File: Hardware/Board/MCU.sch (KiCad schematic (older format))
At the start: 41 parts, among them J3 USB_B_Micro, J5 Conn_ARM_JTAG_SWD_20, SW1 SW_Push, U2 AT25SF081-XMHD-X, Y1 16MHz, Y2 32.768

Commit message: Port Bezeichnungen am Prozessor korrigiert, Schnittstellen angepasst.
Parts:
- removed U2: AT25SF081-XMHD-X, Package_SO:TSSOP-8_4.4x3mm_P0.65mm, symbol Memory_Flash:AT25SF081-XMHD-X
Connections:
- net labels added: CAN1_RX, CAN1_TX, ESP_Boot, ESP_Enable, ESP_Reset, ESP_RxD, ESP_TxD, I2C2_SCL, I2C2_SDA, I2C3_SCL, I2C3_SDA, I2C4_SCL, I2C4_SDA, LPUART_RTS_DE_RS485, LPUART_RX_RX485, LPUART_TX_RS485, OctoSPI_P1_CLK, OctoSPI_P1_DQS, OctoSPI_P1_IO0, OctoSPI_P1_IO1, OctoSPI_P1_IO2, OctoSPI_P1_IO3, OctoSPI_P1_IO4, OctoSPI_P1_IO5, OctoSPI_P1_IO6, OctoSPI_P1_IO7, OctoSPI_P1_NCS, OctoSPI_P2_CLK, OctoSPI_P2_DQS, OctoSPI_P2_IO0, OctoSPI_P2_IO1, OctoSPI_P2_IO2, OctoSPI_P2_IO3, OctoSPI_P2_IO4, OctoSPI_P2_IO5, OctoSPI_P2_IO6, OctoSPI_P2_IO7, OctoSPI_P2_NCS, SLP-LIN1, SLP-LIN2, SLP-LIN3, SPI1_MISO, SPI1_MOSI, SPI1_NSS, SPI1_SCK, STB-CAN, UART4_RX, UART4_TX, UART5_RX, UART5_TX, USART1_RX_LIN1, USART1_TX_LIN1, USART2_RX_LIN2, USART2_TX_LIN2, USART3_RX_LIN3, USART3_TX_LIN3
- net labels removed: Disp_Audio_L, Disp_MOSI, Disp_SCK, OctoSPI_CLK, OctoSPI_DQS, OctoSPI_IO0, OctoSPI_IO1, OctoSPI_IO2, OctoSPI_IO3, OctoSPI_IO4, OctoSPI_IO5, OctoSPI_IO6, OctoSPI_IO7, OctoSPI_NCS, QuadSPI_CLK, QuadSPI_IO0, QuadSPI_IO1, QuadSPI_IO2, QuadSPI_IO3, QuadSPI_NCS, RxD-CAN, RxD-LIN1, RxD-LIN2, RxD-LIN3, RxD-RS485, SCL-1WIRE, SDA-1WIRE, TOUCH_SCL, TOUCH_SDA, TxD-CAN, TxD-LIN1, TxD-LIN2, TxD-LIN3, TxD-RS485
- wire segments 253 -> 291
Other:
- moved on the sheet: D3, J3, U?

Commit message: Octo SPI Flash und RAM zugefügt, weitere Bezeichnungen auf Stand gebracht
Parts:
- removed C14: 100nF, Capacitor_SMD:C_0603_1608Metric, symbol Device:C
- added C? (x6): 100nF, Capacitor_SMD:C_0603_1608Metric, symbol Device:C
- added IC?: IS66WVH8M8BLL-100B1LI_0, BGA24C100P5X5_600X800X120, symbol SamacSys_Parts:IS66WVH8M8BLL-100B1LI_0
- added IC?: MX25LM51245GXDI00, BGA24C100P5X5_600X800X35, symbol SamacSys_Parts:MX25LM51245GXDI00
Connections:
- net labels added: +VSW, LCD_BL_CTRL, LCD_INT, RESET
- net labels removed: Disp_CS, Disp_INT, Disp_MISO
- wire segments 291 -> 334
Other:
- moved on the sheet: D2, D3, J3, J5, U?

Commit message: Eine Menge Arbeit auf der GPN, fast fertig im Schaltplan.
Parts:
- removed D1, D2, D3: SP0504BAJT, Package_TO_SOT_SMD:SOT-353_SC-70-5, symbol Power_Protection:SP0504BAJT
- IC?: symbol SamacSys_Parts:IS66WVH8M8BLL-100B1LI_0 -> Womo-rescue:IS66WVH8M8BLL-100B1LI_0-SamacSys_Parts
- IC?: symbol SamacSys_Parts:MX25LM51245GXDI00 -> Womo-rescue:MX25LM51245GXDI00-SamacSys_Parts
- J?: symbol SamacSys_Parts:54104-4031 -> Womo-rescue:54104-4031-SamacSys_Parts
- J?: symbol SamacSys_Parts:52271-0679 -> Womo-rescue:52271-0679-SamacSys_Parts
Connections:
- net labels added: BLE_INT, Rasp_Shutdown, Rasp_down
- net labels removed: +5VL, BLE_MISO, BLE_MOSI, BLE_RDNY, BLE_REQN, BLE_SCK, Disp_PD, ESP_RxD, ESP_TxD, SLP-LIN1, SLP-LIN2, SLP-LIN3, STB-CAN
- wire segments 334 -> 347
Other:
- moved on the sheet: J3, U?

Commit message: Board to Board Verbindung eingefügt
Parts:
- added C?: 10u, Capacitor_SMD:C_1210_3225Metric, symbol Device:C
- added J?: Conn_02x25_Odd_Even, Connector_PinHeader_2.54mm:PinHeader_2x25_P2.54mm_Vertical, symbol Connector_Generic:Conn_02x25_Odd_Even
- added U?: MOD-nRF8001, RF_Module:MOD-nRF8001, symbol RF_Bluetooth:MOD-nRF8001
- IC1: renamed from IC?; footprint BGA24C100P5X5_600X800X35 -> (none)
- IC2: renamed from IC?; footprint BGA24C100P5X5_600X800X120 -> (none)
- J14: renamed from J?; footprint 52271-0679 -> (none)
- J4: renamed from J?; footprint 54104-4031 -> (none)
- gave numbers to parts that had none: 21
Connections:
- net BLE_Active: now also U?.11 (ACTIVE)
- net BLE_INT: now also U?.10 (RDYN)
- net GND: now also C?.2, J?.43 (Pin_43), J?.44 (Pin_44), J?.49 (Pin_49), J?.50 (Pin_50), U?.2 (GND)
- net LCD_LED-A: now also J?.46 (Pin_46), J?.48 (Pin_48)
- net LCD_LED-K: now also J?.45 (Pin_45), J?.47 (Pin_47)
- net SPI1_MISO: now also U?.9 (MISO)
- net SPI1_MOSI: now also U?.8 (MOSI)
- net SPI1_NSS: now also U?.7 (REQN)
- net SPI1_SCK: now also U?.6 (SCK)
- net PA9: now reaches U17.103 (PA9)
- net PB2: now reaches U17.44 (PB2)
- net PF11: now reaches U17.45 (PF11)
- new net +3.3VA: C?.1, U?.1 (3V3)
- new net BLE_RST: U?.3 (RST)
- no-connect marks 0 -> 2
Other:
- note added: "Connection to Mainboard"
- moved on the sheet: BT1, C1, C10, C11, C12, C13, C15, C2, C3, C4, C5, C6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

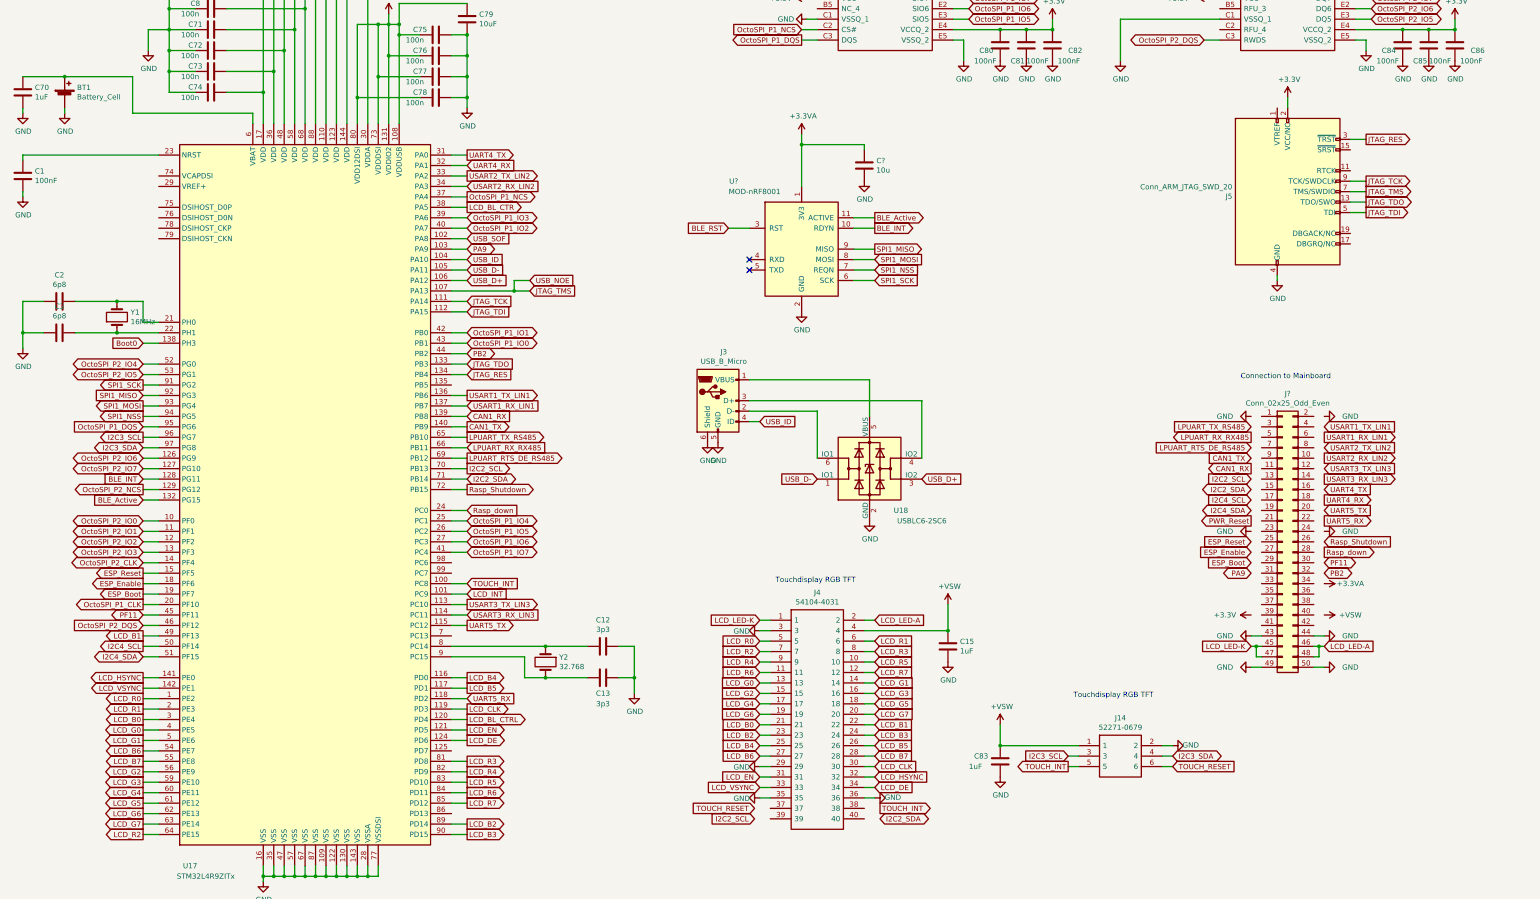
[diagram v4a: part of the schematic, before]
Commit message: Resitiven Touch Controller eingefügt, diverse I2C Parts hinzu gefügt, Netze umgenannt
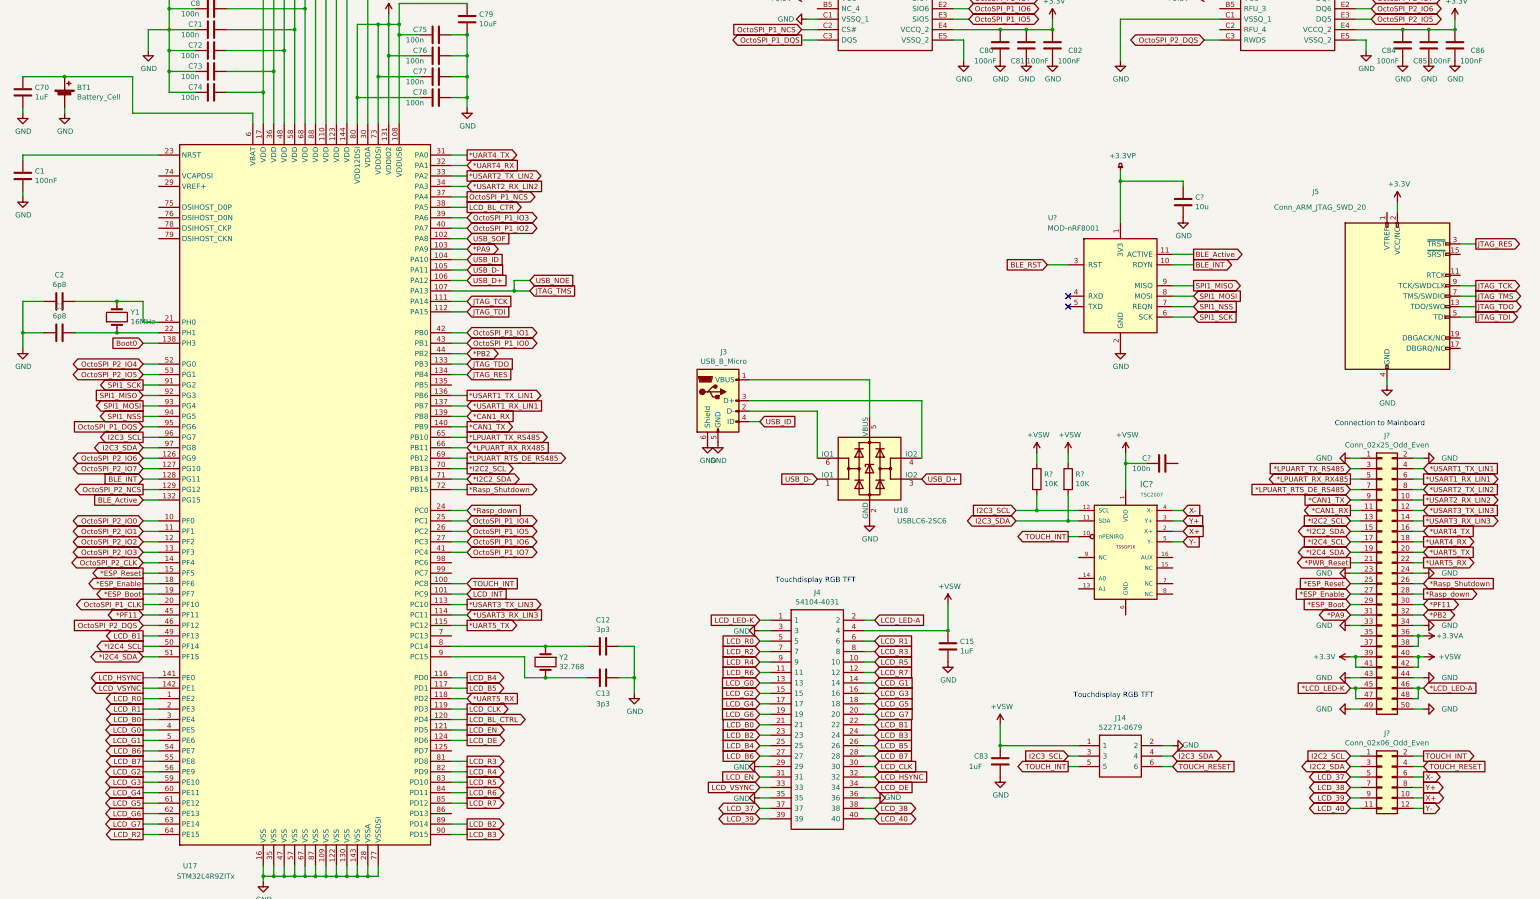
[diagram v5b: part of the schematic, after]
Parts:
- added C?: 100n, Capacitor_SMD:C_0603_1608Metric, symbol Device:C
- added IC?: TSC2007, symbol opendous:TSC2007
- added J?: Conn_02x06_Odd_Even, symbol Connector_Generic:Conn_02x06_Odd_Even
- added R? (x2): 10K, Resistor_SMD:R_0603_1608Metric, symbol Device:R
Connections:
- net CAN1_RX is gone; now on net *CAN1_RX: U17.139 (PB8)
- net CAN1_TX is gone; now on net *CAN1_TX: U17.140 (PB9)
- net ESP_Boot is gone; now on net *ESP_Boot: U17.19 (PF7)
- net ESP_Enable is gone; now on net *ESP_Enable: U17.18 (PF6)
- net ESP_Reset is gone; now on net *ESP_Reset: U17.15 (PF5)
- net I2C4_SCL is gone; now on net *I2C4_SCL: U17.50 (PF14)
- net I2C4_SDA is gone; now on net *I2C4_SDA: U17.51 (PF15)
- net LPUART_RTS_DE_RS485 is gone; now on net *LPUART_RTS_DE_RS485: U17.69 (PB12)
- net LPUART_RX_RX485 is gone; now on net *LPUART_RX_RX485: U17.66 (PB11)
- net LPUART_TX_RS485 is gone; now on net *LPUART_TX_RS485: U17.65 (PB10)
- net PA9 is gone; now on net *PA9: U17.103 (PA9)
- net PB2 is gone; now on net *PB2: U17.44 (PB2)
- net PF11 is gone; now on net *PF11: U17.45 (PF11)
- net Rasp_Shutdown is gone; now on net *Rasp_Shutdown: U17.72 (PB15)
- net Rasp_down is gone; now on net *Rasp_down: U17.24 (PC0)
- net UART4_RX is gone; now on net *UART4_RX: U17.32 (PA1)
- net UART4_TX is gone; now on net *UART4_TX: U17.31 (PA0)
- net UART5_RX is gone; now on net *UART5_RX: U17.118 (PD2)
- net UART5_TX is gone; now on net *UART5_TX: U17.115 (PC12)
- net USART1_RX_LIN1 is gone; now on net *USART1_RX_LIN1: U17.137 (PB7)
- net USART1_TX_LIN1 is gone; now on net *USART1_TX_LIN1: U17.136 (PB6)
- net USART2_RX_LIN2 is gone; now on net *USART2_RX_LIN2: U17.34 (PA3)
- net USART2_TX_LIN2 is gone; now on net *USART2_TX_LIN2: U17.33 (PA2)
- net USART3_RX_LIN3 is gone; now on net *USART3_RX_LIN3: U17.114 (PC11)
- net USART3_TX_LIN3 is gone; now on net *USART3_TX_LIN3: U17.113 (PC10)
- net +3.3VA: now also J?.36 (Pin_36), J?.38 (Pin_38); no longer C?.1, U?.1 (3V3)
- net +3V3: now also J?.39 (Pin_39), J?.41 (Pin_41)
- net +VSW: now also J?.40 (Pin_40), J?.42 (Pin_42), C?.2, IC?.1 (VDD), R?.1, R?.1
- net GND: now also J?.1 (Pin_1), J?.2 (Pin_2), J?.23 (Pin_23), J?.24 (Pin_24), J?.33 (Pin_33), J?.34 (Pin_34)
- net I2C2_SCL: now also J?.1 (Pin_1); no longer U17.70 (PB13)
- net I2C2_SDA: now also J?.3 (Pin_3); no longer U17.71 (PB14)
- net I2C3_SCL: now also IC?.12 (SCL), R?.2
- net I2C3_SDA: now also IC?.11 (SDA), R?.2
- net LCD_LED-A: no longer J?.46 (Pin_46), J?.48 (Pin_48)
- net LCD_LED-K: no longer J?.45 (Pin_45), J?.47 (Pin_47)
- net TOUCH_INT: now also IC?.10 (nPENIRQ), J?.2 (Pin_2)
- net TOUCH_RESET: now also J?.4 (Pin_4)
- net LCD_37: now reaches J4.37
- net LCD_37: now also J?.5 (Pin_5)
- net LCD_38: now reaches J4.38
- net LCD_38: now also J?.7 (Pin_7)
- net LCD_39: now reaches J4.39
- net LCD_39: now also J?.9 (Pin_9)
- net LCD_40: now reaches J4.40
- net LCD_40: now also J?.11 (Pin_11)
- net *USART2_RX_LIN2: now reaches J?.10 (Pin_10)
- net *CAN1_RX: now reaches J?.11 (Pin_11)
- net *USART3_TX_LIN3: now reaches J?.12 (Pin_12)
- net *I2C2_SCL: now reaches J?.13 (Pin_13)
- net *I2C2_SCL: now also U17.70 (PB13)
- net *USART3_RX_LIN3: now reaches J?.14 (Pin_14)
- net *I2C2_SDA: now reaches J?.15 (Pin_15)
- net *I2C2_SDA: now also U17.71 (PB14)
- net *UART4_TX: now reaches J?.16 (Pin_16)
- net *I2C4_SCL: now reaches J?.17 (Pin_17)
- net *UART4_RX: now reaches J?.18 (Pin_18)
- net *I2C4_SDA: now reaches J?.19 (Pin_19)
- net *UART5_TX: now reaches J?.20 (Pin_20)
- net *PWR_Reset: now reaches J?.21 (Pin_21)
- net *UART5_RX: now reaches J?.22 (Pin_22)
- net *ESP_Reset: now reaches J?.25 (Pin_25)
- net *Rasp_Shutdown: now reaches J?.26 (Pin_26)
- net *ESP_Enable: now reaches J?.27 (Pin_27)
- net *Rasp_down: now reaches J?.28 (Pin_28)
- net *ESP_Boot: now reaches J?.29 (Pin_29)
- net *LPUART_TX_RS485: now reaches J?.3 (Pin_3)
- net *PF11: now reaches J?.30 (Pin_30)
- net *PA9: now reaches J?.31 (Pin_31)
- net *PB2: now reaches J?.32 (Pin_32)
- net *USART1_TX_LIN1: now reaches J?.4 (Pin_4)
- net *LPUART_RX_RX485: now reaches J?.5 (Pin_5)
- net *USART1_RX_LIN1: now reaches J?.6 (Pin_6)
- net *LPUART_RTS_DE_RS485: now reaches J?.7 (Pin_7)
- net *USART2_TX_LIN2: now reaches J?.8 (Pin_8)
- net *CAN1_TX: now reaches J?.9 (Pin_9)
- new net *LCD_LED-A: J?.46 (Pin_46), J?.48 (Pin_48)
- new net *LCD_LED-K: J?.45 (Pin_45), J?.47 (Pin_47)
- new net +3.3VP: C?.1, U?.1 (3V3)
- new net X+: IC?.2 (X+), J?.10 (Pin_10)
- new net X-: IC?.4 (X-), J?.6 (Pin_6)
- new net Y+: IC?.3 (Y+), J?.8 (Pin_8)
- new net Y-: IC?.5 (Y-), J?.12 (Pin_12)
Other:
- moved on the sheet: C?, J5, J?, U?

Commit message: GSM Modul SIM800L eingefügt, Spannung MCU Board umgenannt
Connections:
- net +3.3VP is gone; now on net +3.3VA: C?.1, U?.1 (3V3)
- net GND: no longer BT1.2 (-), C1.2, C10.2, C11.2, C12.1, C13.1, C15.2, C2.2, C3.2, C4.2, C5.2, C6.2, C7.2, C70.2, C71.2, C72.2, C73.2, C74.2, C75.1, C76.1, C77.1, C78.1, C79.2, C8.2, C80.2, C81.2, C82.2, C83.2, C84.2, C85.2, C86.2, C9.2, C?.2, IC1.B3 (GND), IC1.C1 (VSSQ_1), IC1.E5 (VSSQ_2), IC2.B3 (VSS), IC2.C1 (VSSQ_1), IC2.E5 (VSSQ_2), J14.2, J3.5 (GND), J3.6 (Shield), J4.29, J4.3, J4.35, J4.36, J5.10 (GND), J5.12 (GND), J5.14 (GND), J5.16 (GND), J5.18 (GND), J5.20 (GND), J5.4 (GND), J5.6 (GND), J5.8 (GND), J?.1 (Pin_1), J?.2 (Pin_2), J?.33 (Pin_33), J?.34 (Pin_34), J?.43 (Pin_43), J?.44 (Pin_44), J?.49 (Pin_49), J?.50 (Pin_50), U17.109 (VSS), U17.122 (VSS), U17.130 (VSS), U17.143 (VSS), U17.16 (VSS), U17.28 (VSSA), U17.35 (VSS), U17.47 (VSS), U17.57 (VSS), U17.67 (VSS), U17.77 (VSSDSI), U17.87 (VSS), U18.2 (GND), U?.2 (GND)
- net GND1: now reaches IC?.13 (A1)
- net GND1: now also BT1.2 (-), C1.2, C10.2, C11.2, C12.1, C13.1, C15.2, C2.2, C3.2, C4.2, C5.2, C6.2, C7.2, C70.2, C71.2, C72.2, C73.2, C74.2, C75.1, C76.1, C77.1, C78.1, C79.2, C8.2, C80.2, C81.2, C82.2, C83.2, C84.2, C85.2, C86.2, C9.2, C?.1, C?.2, IC1.B3 (GND), IC1.C1 (VSSQ_1), IC1.E5 (VSSQ_2), IC2.B3 (VSS), IC2.C1 (VSSQ_1), IC2.E5 (VSSQ_2), IC?.14 (A0), IC?.6 (GND), J14.2, J3.5 (GND), J3.6 (Shield), J4.29, J4.3, J4.35, J4.36, J5.10 (GND), J5.12 (GND), J5.14 (GND), J5.16 (GND), J5.18 (GND), J5.20 (GND), J5.4 (GND), J5.6 (GND), J5.8 (GND), J?.1 (Pin_1), J?.2 (Pin_2), J?.33 (Pin_33), J?.34 (Pin_34), J?.43 (Pin_43), J?.44 (Pin_44), J?.49 (Pin_49), J?.50 (Pin_50), U17.109 (VSS), U17.122 (VSS), U17.130 (VSS), U17.143 (VSS), U17.16 (VSS), U17.28 (VSSA), U17.35 (VSS), U17.47 (VSS), U17.57 (VSS), U17.67 (VSS), U17.77 (VSSDSI), U17.87 (VSS), U18.2 (GND), U?.2 (GND)
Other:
- note added: "Touchconfig"
- note added: "Touchcontroller"
- moved on the sheet: J?

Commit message: MCU Section fertig, Analog Inputs angelegt, Schaltplan neu organisiert, alte Datenblätter entfernt.
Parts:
- removed FB18: Ferrite_Bead_Small, symbol Device:Ferrite_Bead_Small
- added C? (x4): 1uF, Capacitor_SMD:C_0603_1608Metric, symbol Device:C
- added FB? (x5): Ferrite, symbol Device:Ferrite_Bead_Small
- added R?: 10K, Resistor_SMD:R_0603_1608Metric, symbol Device:R
- added SW?: SW_Push, symbol Switch:SW_Push
- C78: value 100n -> 2u2
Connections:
- net *LCD_LED-A: now also FB?.2; no longer J?.46 (Pin_46), J?.48 (Pin_48)
- net *LCD_LED-K: now also FB?.1; no longer J?.45 (Pin_45), J?.47 (Pin_47)
- net +3.3VA: now also C?.1, FB?.2; no longer J?.36 (Pin_36), J?.38 (Pin_38)
- net +3V3: now also C10.1, C11.1, U17.29 (VREF+), U17.30 (VDDA), C?.1, C?.1, FB?.1, SW?.2; no longer C78.2, J?.39 (Pin_39), J?.41 (Pin_41), U17.80 (VDD12DSI)
- net +VSW: now also C?.1, FB?.2; no longer J?.40 (Pin_40), J?.42 (Pin_42)
- net Boot0: now also R?.1, SW?.1
- net GND1: now also SW1.1, C?.2, C?.2, C?.2, C?.2, R?.2
- net RESET: now also C1.1, C78.2, SW1.2, U17.23 (NRST), U17.74 (VCAPDSI), U17.80 (VDD12DSI)
- net *PC6: now reaches U17.98 (PC6)
- net *PC6: now also J?.35 (Pin_35)
- net *PC7: now reaches U17.99 (PC7)
- net *PC7: now also J?.37 (Pin_37)
- new net: FB?.1, J?.36 (Pin_36), J?.38 (Pin_38)
- new net: FB?.2, J?.39 (Pin_39), J?.41 (Pin_41)
- new net: FB?.1, J?.40 (Pin_40), J?.42 (Pin_42)
- new net: FB?.2, J?.45 (Pin_45), J?.47 (Pin_47)
- new net: FB?.1, J?.46 (Pin_46), J?.48 (Pin_48)
- no-connect marks 2 -> 23
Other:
- note added: "I2C ADR: 1001000"
- moved on the sheet: C10, C11, C4, C5, C6, C7, C71, C72, C73, C74, C75, C76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

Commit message: Trennung MCU und Rest, Footprints fast alles zugewiesen, GSM Modul integriert, viel Kleinkram
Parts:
- added D19: LED, LED_SMD:LED_1206_3216Metric, symbol Device:LED
- added R76: 10K, Resistor_SMD:R_0603_1608Metric, symbol Device:R
- added SW3: SW_Push, symbol Switch:SW_Push
- BT1: footprint (none) -> Battery:BatteryHolder_Keystone_1058_1x2032
- FB45, FB46, FB47, FB48, FB49: renamed from FB?; footprint (none) -> Inductor_SMD:L_0603_1608Metric
- IC1, IC2: footprint (none) -> SamacSys_Parts:BGA24C100P5X5_600X800X35
- IC3: renamed from IC?; footprint (none) -> Package_SO:TSSOP-16_4.4x5mm_P0.65mm
- J14: footprint (none) -> SamacSys_Parts:52271-0679
- J22: renamed from J?; footprint (none) -> Connector_PinHeader_2.54mm:PinHeader_2x06_P2.54mm_Vertical
- J4: footprint (none) -> SamacSys_Parts:54104-4031
- gave numbers to parts that had none: 12
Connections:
- net +3V3: now also R76.1
- net GND1: now also D19.1 (K), SW3.1; no longer R75.2
- net Wakeup: now reaches U17.135 (PB5)
- net Wakeup: now also R76.2, SW3.2
- net Signal_LED: now reaches U17.7 (PC13)
- net Signal_LED: now also D19.2 (A)
